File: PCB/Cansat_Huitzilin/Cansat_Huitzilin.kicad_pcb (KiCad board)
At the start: 4 copper layers, 59 x 59 mm, 84 parts, among them IC1 AP64501SP-13, IC2 114993390, IC3 BMM350, IC4 BMI323, IC5 STCC4-D-R3, IC6 SHT40-AD1B-R2, J1 Screw_Terminal_01x02, J2 Conn_01x04, J3 Conn_01x03, J4 Conn_01x06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

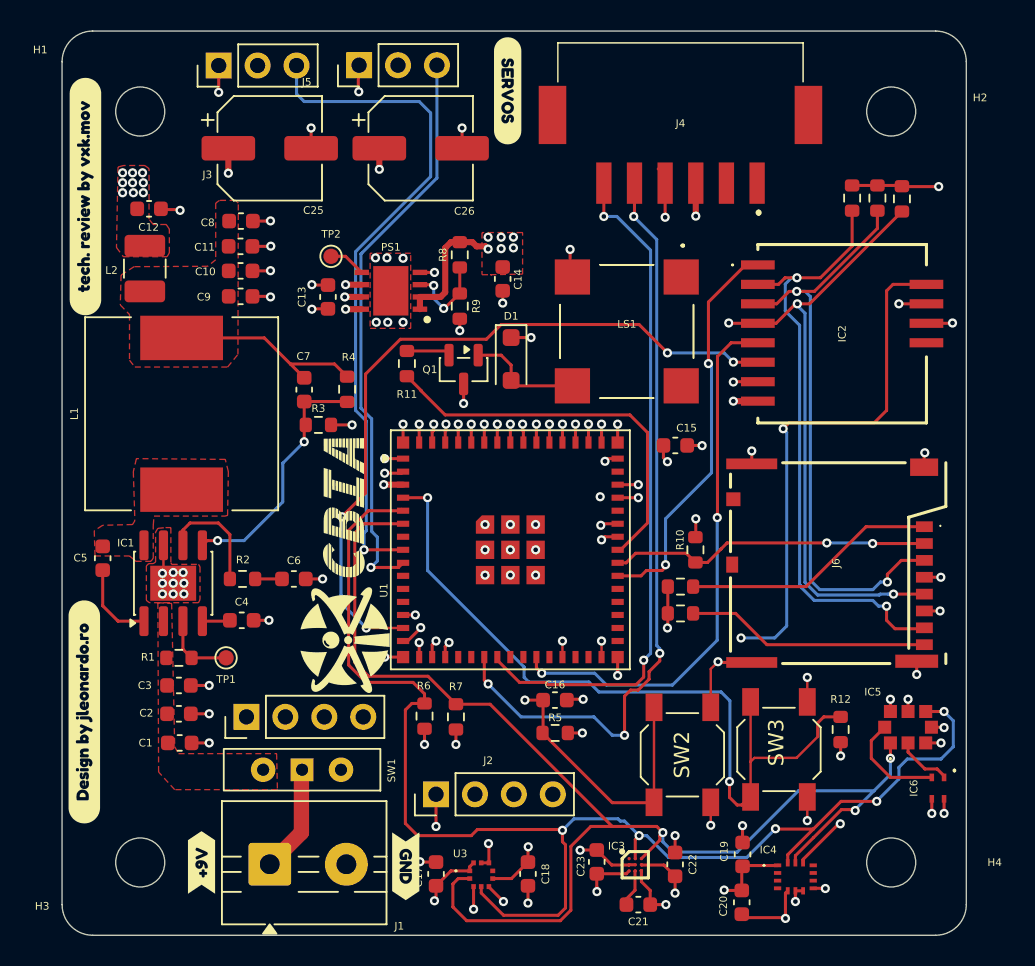
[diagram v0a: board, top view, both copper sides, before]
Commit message: GUI & PCB
Complete Mission Control v1.0.1 and integrate final CanSat PCB + libraries
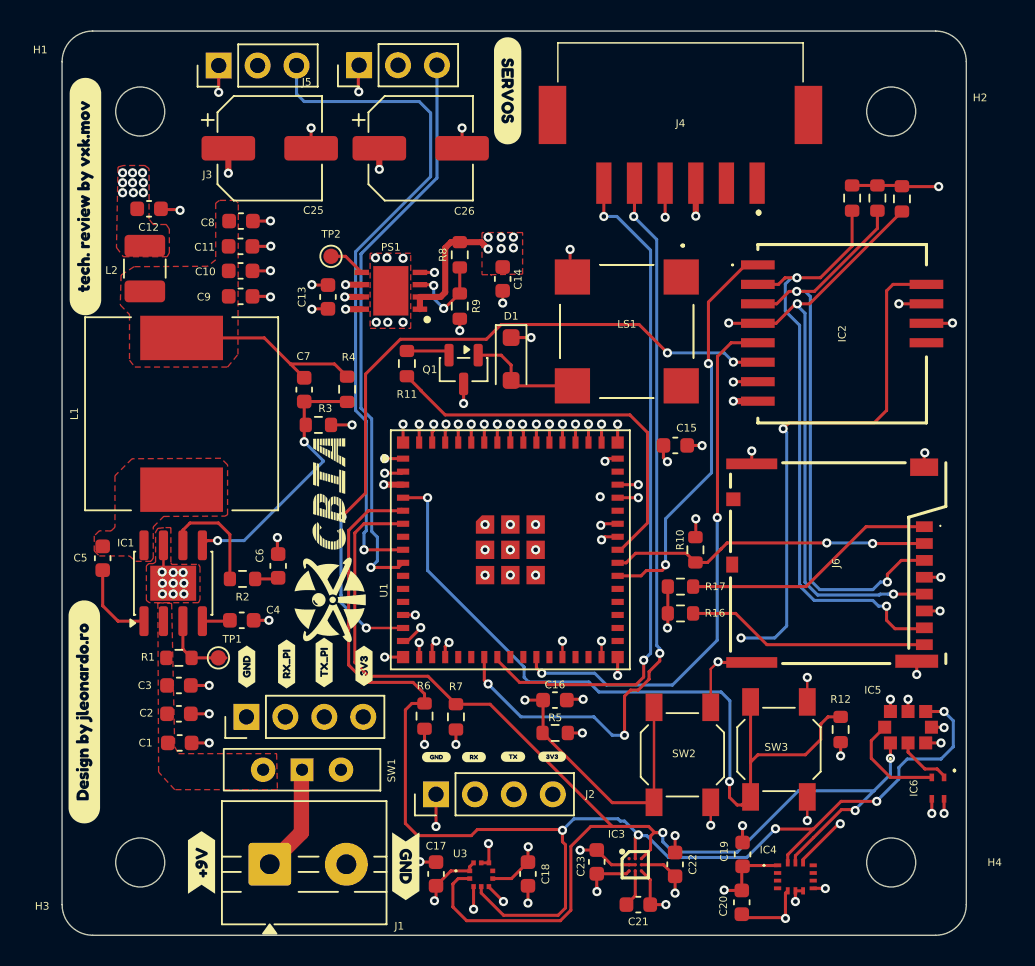
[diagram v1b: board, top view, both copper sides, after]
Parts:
- added kibuzzard-69ADC2FE: G***, kibuzzard-69ADC2FE, F.Cu at (83.0, 79.5)
- added kibuzzard-69ADC375: G***, kibuzzard-69ADC375, F.Cu at (85.7, 79.3)
- added kibuzzard-69ADC389: G***, kibuzzard-69ADC389, F.Cu at (88.1, 79.2)
- added kibuzzard-69ADC3B5: G***, kibuzzard-69ADC3B5, F.Cu at (90.7, 79.4)
- added kibuzzard-69ADC45A: G***, kibuzzard-69ADC45A, F.Cu at (95.4, 85.4)
- added kibuzzard-69ADC495: G***, kibuzzard-69ADC495, F.Cu at (97.9, 85.4)
- added kibuzzard-69ADC49F: G***, kibuzzard-69ADC49F, F.Cu at (100.4, 85.3)
- added kibuzzard-69ADC4A7: G***, kibuzzard-69ADC4A7, F.Cu at (103.0, 85.3)
- moved G*** 1.87 mm to (88.5, 71.0)
- moved C6 1.33 mm to (85.1, 72.9), turned to 90 degrees
- moved TP1 0.50 mm to (81.2, 78.9)
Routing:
- net Net-(IC1-FB): track 16.3 -> 17.4 mm

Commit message: save
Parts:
- removed IC5: STCC4-D-R3, SamacSys_Parts:STCC4DR3
- removed IC6: SHT40-AD1B-R2, SamacSys_Parts:SHT40AD1BR2
- removed kibuzzard-69ACDC7E: G***, kibuzzard-69ACDC7E
- added kibuzzard-69CE0A89: G***, kibuzzard-69CE0A89, F.Cu at (72.3, 49.5)
- added kibuzzard-69CE31E7: G***, kibuzzard-69CE31E7, F.Cu at (119.3, 49.9)
- H1, H2, H3, H4: footprint MountingHole:MountingHole_3.2mm_M3 -> MountingHole:MountingHole_3.2mm_M3_Pad_Via
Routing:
- net SDA: track 89.4 -> 70.8 mm, vias 5 -> 3
- net SCL: track 85.0 -> 73.2 mm, vias 3 -> 2
- net SCL_SHT4: track 6.86 -> 0.00 mm
- net Net-(IC5-SDA_C): track 3.69 -> 0.00 mm
- net GND: track 101.4 -> 98.7 mm, vias 94 -> 91
- net +3.3V: track 54.9 -> 53.4 mm, vias 28 -> 24
- net Net-(IC1-FB): track 17.4 -> 16.3 mm
